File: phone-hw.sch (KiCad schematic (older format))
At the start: 45 parts

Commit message: connect RI to esp32
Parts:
- added R?: 10k, Resistor_SMD:R_0603_1608Metric_Pad1.05x0.95mm_HandSolder, symbol Device:R_Small_US
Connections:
- net labels added: GSM_RI, GSM_RI_2.8
- wire segments 333 -> 341
- no-connect marks 14 -> 11
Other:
- moved on the sheet: J?
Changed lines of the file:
@@
 F7 "DBG_RXD" I L 8450 1150 50
 F8 "PWRKEY" I R 9600 900 50
+F9 "RI" O R 9600 1300 50
 $EndSheet
 $Comp
@@
 	7450 4150 7450 4250
 Wire Wire Line
-	6900 4200 6900 4250
-Wire Wire Line
-	6900 4250 7100 4250
-Wire Wire Line
 	7100 4250 7450 4250
-Connection ~ 7100 4250
 $Comp
 L Device:R_Small_US R?
@@
 L power:VDD #PWR?
 U 1 1 5CF832E7
-P 4800 3500
-F 0 "#PWR?" H 4800 3350 50  0001 C CNN
-F 1 "VDD" H 4817 3673 50  0000 C CNN
-F 2 "" H 4800 3500 50  0001 C CNN
-F 3 "" H 4800 3500 50  0001 C CNN
-	1    4800 3500
+P 4800 3450
+F 0 "#PWR?" H 4800 3300 50  0001 C CNN
+F 1 "VDD" H 4817 3623 50  0000 C CNN
+F 2 "" H 4800 3450 50  0001 C CNN
+F 3 "" H 4800 3450 50  0001 C CNN
+	1    4800 3450
 	1    0    0    -1
 $EndComp
@@
 L power:+BATT #PWR?
 U 1 1 5CF9532A
-P 6900 4200
-F 0 "#PWR?" H 6900 4050 50  0001 C CNN
-F 1 "+BATT" H 6915 4373 50  0000 C CNN
-F 2 "" H 6900 4200 50  0001 C CNN
-F 3 "" H 6900 4200 50  0001 C CNN
-	1    6900 4200
+P 7750 4200
+F 0 "#PWR?" H 7750 4050 50  0001 C CNN
+F 1 "+BATT" H 7765 4373 50  0000 C CNN
+F 2 "" H 7750 4200 50  0001 C CNN
+F 3 "" H 7750 4200 50  0001 C CNN
+	1    7750 4200
 	1    0    0    -1
 $EndComp
 Wire Wire Line
 	6650 3600 7200 3600
-NoConn ~ 5850 4000
 NoConn ~ 5850 4100
 NoConn ~ 6650 4100
-NoConn ~ 6650 4000
 Wire Wire Line
 	8150 950  8250 950
@@
 Wire Wire Line
 	8400 4400 8400 4900
-Text GLabel 3550 4100 0    39   Output ~ 0
+Text GLabel 3900 4850 0    39   Output ~ 0
 JTAG_MTDO
-Text GLabel 3550 3900 0    39   Input ~ 0
+Text GLabel 3900 4650 0    39   Input ~ 0
 JTAG_MTCK
-Text GLabel 3550 4000 0    39   Input ~ 0
+Text GLabel 3900 4750 0    39   Input ~ 0
 JTAG_MTMS
-Text GLabel 3550 3800 0    39   Input ~ 0
+Text GLabel 3900 4550 0    39   Input ~ 0
 JTAG_MTDI
 Wire Wire Line
-	3550 4100 3600 4100
-Wire Wire Line
-	3600 4000 3550 4000
-Wire Wire Line
-	3550 3900 3600 3900
-Wire Wire Line
-	3550 3800 3600 3800
+	3900 4850 3950 4850
+Wire Wire Line
+	3950 4750 3900 4750
+Wire Wire Line
+	3900 4650 3950 4650
+Wire Wire Line
+	3900 4550 3950 4550
 $Comp
 L Connector_Generic:Conn_01x06 J?
 U 1 1 5D4CA230
-P 3800 3900
-F 0 "J?" H 4100 3950 50  0000 C CNN
-F 1 "Conn_01x06" H 4100 3850 50  0000 C CNN
-F 2 "Connector_PinHeader_2.54mm:PinHeader_1x06_P2.54mm_Vertical" H 3800 3900 50  0001 C CNN
-F 3 "~" H 3800 3900 50  0001 C CNN
-	1    3800 3900
+P 4150 4650
+F 0 "J?" H 4450 4700 50  0000 C CNN
+F 1 "Conn_01x06" H 4450 4600 50  0000 C CNN
+F 2 "Connector_PinHeader_2.54mm:PinHeader_1x06_P2.54mm_Vertical" H 4150 4650 50  0001 C CNN
+F 3 "~" H 4150 4650 50  0001 C CNN
+	1    4150 4650
 	1    0    0    -1
 $EndComp
@@
 L power:GND #PWR?
 U 1 1 5DC8B84C
-P 3550 4250
-F 0 "#PWR?" H 3550 4000 50  0001 C CNN
-F 1 "GND" H 3555 4077 50  0000 C CNN
-F 2 "" H 3550 4250 50  0001 C CNN
-F 3 "" H 3550 4250 50  0001 C CNN
-	1    3550 4250
-	1    0    0    -1
-$EndComp
-Wire Wire Line
-	3600 4200 3550 4200
-Wire Wire Line
-	3550 4200 3550 4250
+P 3900 5000
+F 0 "#PWR?" H 3900 4750 50  0001 C CNN
+F 1 "GND" H 3905 4827 50  0000 C CNN
+F 2 "" H 3900 5000 50  0001 C CNN
+F 3 "" H 3900 5000 50  0001 C CNN
+	1    3900 5000
+	1    0    0    -1
+$EndComp
+Wire Wire Line
+	3950 4950 3900 4950
+Wire Wire Line
+	3900 4950 3900 5000
 $Comp
 L power:VDD #PWR?
 U 1 1 5DCA34FE
-P 3550 3650
-F 0 "#PWR?" H 3550 3500 50  0001 C CNN
-F 1 "VDD" H 3567 3823 50  0000 C CNN
-F 2 "" H 3550 3650 50  0001 C CNN
-F 3 "" H 3550 3650 50  0001 C CNN
-	1    3550 3650
-	1    0    0    -1
-$EndComp
-Wire Wire Line
-	3600 3700 3550 3700
-Wire Wire Line
-	3550 3700 3550 3650
+P 3900 4400
+F 0 "#PWR?" H 3900 4250 50  0001 C CNN
+F 1 "VDD" H 3917 4573 50  0000 C CNN
+F 2 "" H 3900 4400 50  0001 C CNN
+F 3 "" H 3900 4400 50  0001 C CNN
+	1    3900 4400
+	1    0    0    -1
+$EndComp
+Wire Wire Line
+	3950 4450 3900 4450
+Wire Wire Line
+	3900 4450 3900 4400
 $Comp
 L Device:R_Small_US R?
@@
 	1    0    0    -1
 $EndComp
-NoConn ~ 2550 4800
+Text GLabel 9700 1300 2    39   Output ~ 0
+GSM_RI
+Wire Wire Line
+	9600 1300 9700 1300
+Text GLabel 6700 4000 2    39   Input ~ 0
+GSM_RI
+Wire Wire Line
+	7450 4250 7750 4250
+Wire Wire Line
+	7750 4250 7750 4200
+Connection ~ 7450 4250
+Wire Wire Line
+	6650 4000 6700 4000
+Text GLabel 4200 4000 0    39   Output ~ 0
+GSM_RI_2.8
+Wire Wire Line
+	5850 4000 4350 4000
+$Comp
+L Device:R_Small_US R?
+U 1 1 5DC1E4EB
+P 4350 3750
+F 0 "R?" H 4418 3796 50  0000 L CNN
+F 1 "10k" H 4418 3705 50  0000 L CNN
+F 2 "Resistor_SMD:R_0603_1608Metric_Pad1.05x0.95mm_HandSolder" H 4350 3750 50  0001 C CNN
+F 3 "~" H 4350 3750 50  0001 C CNN
+	1    4350 3750
+	-1   0    0    -1
+$EndComp
+Wire Wire Line
+	4350 4000 4350 3850
+Connection ~ 4350 4000
+Wire Wire Line
+	4350 4000 4200 4000
+Wire Wire Line
+	4800 3500 4350 3500
+Wire Wire Line
+	4350 3500 4350 3650
+Connection ~ 4800 3500
+Wire Wire Line
+	4800 3500 4800 3450
+Text GLabel 2550 4800 2    39   Input ~ 0
+GSM_RI_2.8
 $EndSCHEMATC

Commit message: annotate schematic and tweak some footprint associations
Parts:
- SW4, SW5, SW6: renamed from SW?; footprint Button_Switch_SMD:SW_SPST_EVQPE1 -> Button_Switch_THT:SW_Tactile_SPST_Angled_PTS645Vx58-2LFS
- U2: renamed from U?; footprint (none) -> Package_SO:TSSOP-24_4.4x7.8mm_P0.65mm
- gave numbers to parts that had none: 42

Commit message: change battery to use two different connectors instead of a small pin header
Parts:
- removed BT1: Battery_Cell, Connector_PinHeader_2.54mm:PinHeader_1x02_P2.54mm_Vertical, symbol Device:Battery_Cell
- added J5: BATT+, symbol Connector:Conn_01x01_Female
- added J6: BATT-, symbol Connector:Conn_01x01_Female
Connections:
- wire segments 341 -> 339
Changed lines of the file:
@@
 	2900 1050 2900 900
-Wire Wire Line
-	2300 900  2300 950
-$Comp
-L Device:Battery_Cell BT1
-U 1 1 5C9332A7
-P 2300 1150
-F 0 "BT1" H 2418 1246 50  0000 L CNN
-F 1 "Battery_Cell" H 2418 1155 50  0000 L CNN
-F 2 "Connector_PinHeader_2.54mm:PinHeader_1x02_P2.54mm_Vertical" V 2300 1210 50  0001 C CNN
-F 3 "~" V 2300 1210 50  0001 C CNN
-	1    2300 1150
-	1    0    0    -1
-$EndComp
-Wire Wire Line
-	2300 1250 2300 1300
 Wire Wire Line
 	2900 1300 2900 1150
@@
 Wire Wire Line
 	1200 4900 1250 4900
-Wire Wire Line
-	2300 900  2900 900
-Wire Wire Line
-	2300 1300 2900 1300
-$Comp
-L power:PWR_FLAG #FLG01
-U 1 1 5D6F8FE7
-P 1950 1250
-F 0 "#FLG01" H 1950 1325 50  0001 C CNN
-F 1 "PWR_FLAG" H 1950 1423 50  0000 C CNN
-F 2 "" H 1950 1250 50  0001 C CNN
-F 3 "~" H 1950 1250 50  0001 C CNN
-	1    1950 1250
-	1    0    0    -1
-$EndComp
-Wire Wire Line
-	2300 1300 1950 1300
-Wire Wire Line
-	1950 1300 1950 1250
-Connection ~ 2300 1300
 $Comp
 L power:PWR_FLAG #FLG03
@@
 Text GLabel 2550 4800 2    39   Input ~ 0
 GSM_RI_2.8
+$Comp
+L Connector:Conn_01x01_Female J5
+U 1 1 5DE9CCC6
+P 2100 900
+F 0 "J5" H 1992 675 50  0000 C CNN
+F 1 "BATT+" H 1992 766 50  0000 C CNN
+F 2 "" H 2100 900 50  0001 C CNN
+F 3 "~" H 2100 900 50  0001 C CNN
+	1    2100 900
+	-1   0    0    1
+$EndComp
+$Comp
+L Connector:Conn_01x01_Female J6
+U 1 1 5DF18DEB
+P 2100 1300
+F 0 "J6" H 1992 1075 50  0000 C CNN
+F 1 "BATT-" H 1992 1166 50  0000 C CNN
+F 2 "" H 2100 1300 50  0001 C CNN
+F 3 "~" H 2100 1300 50  0001 C CNN
+	1    2100 1300
+	-1   0    0    1
+$EndComp
+Wire Wire Line
+	2300 1300 2700 1300
+$Comp
+L power:PWR_FLAG #FLG0102
+U 1 1 5DF195A7
+P 2700 1200
+F 0 "#FLG0102" H 2700 1275 50  0001 C CNN
+F 1 "PWR_FLAG" H 2700 1373 50  0000 C CNN
+F 2 "" H 2700 1200 50  0001 C CNN
+F 3 "~" H 2700 1200 50  0001 C CNN
+	1    2700 1200
+	1    0    0    -1
+$EndComp
+Wire Wire Line
+	2700 1200 2700 1300
+Connection ~ 2700 1300
+Wire Wire Line
+	2700 1300 2900 1300
+Wire Wire Line
+	2300 900  2900 900
 $EndSCHEMATC

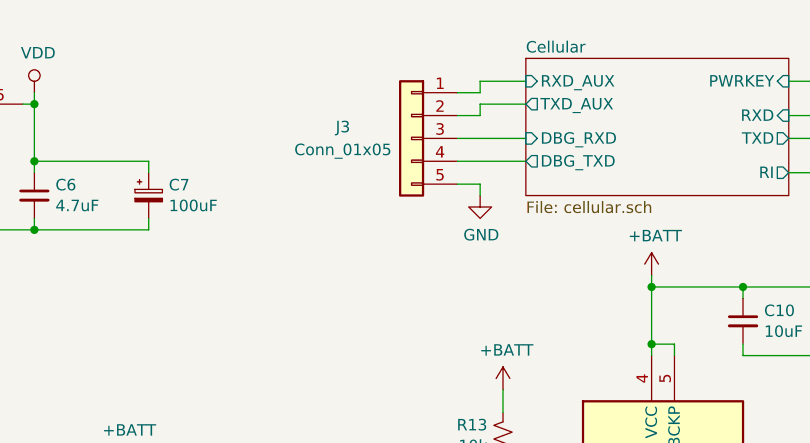
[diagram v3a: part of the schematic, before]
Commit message: remove debug port for modem
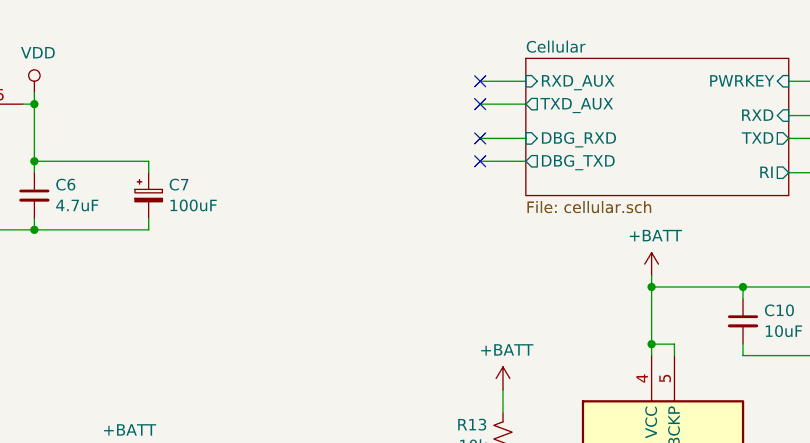
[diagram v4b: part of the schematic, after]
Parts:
- removed J3: Conn_01x05, Connector_PinHeader_2.54mm:PinHeader_1x05_P2.54mm_Vertical, symbol Connector_Generic:Conn_01x05
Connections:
- no-connect marks 11 -> 15
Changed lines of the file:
@@
 NoConn ~ 6650 4100
 Wire Wire Line
-	8150 950  8250 950
-Wire Wire Line
-	8250 950  8250 900
-Wire Wire Line
 	8250 900  8450 900
 Wire Wire Line
-	8150 1050 8250 1050
-Wire Wire Line
-	8250 1050 8250 1000
-Wire Wire Line
 	8250 1000 8450 1000
-Wire Wire Line
-	8150 1150 8450 1150
-Wire Wire Line
-	8150 1250 8450 1250
 $Comp
 L power:PWR_FLAG #FLG02
@@
 	-1   0    0    -1
 $EndComp
-$Comp
-L Connector_Generic:Conn_01x05 J3
-U 1 1 5D00D675
-P 7950 1150
-F 0 "J3" H 8250 1200 50  0000 C CNN
-F 1 "Conn_01x05" H 8250 1100 50  0000 C CNN
-F 2 "Connector_PinHeader_2.54mm:PinHeader_1x05_P2.54mm_Vertical" H 7950 1150 50  0001 C CNN
-F 3 "~" H 7950 1150 50  0001 C CNN
-	1    7950 1150
-	-1   0    0    -1
-$EndComp
-$Comp
-L power:GND #PWR044
-U 1 1 5DC175EF
-P 8250 1400
-F 0 "#PWR044" H 8250 1150 50  0001 C CNN
-F 1 "GND" H 8255 1227 50  0000 C CNN
-F 2 "" H 8250 1400 50  0001 C CNN
-F 3 "" H 8250 1400 50  0001 C CNN
-	1    8250 1400
-	1    0    0    -1
-$EndComp
-Wire Wire Line
-	8150 1350 8250 1350
-Wire Wire Line
-	8250 1350 8250 1400
 $Comp
 L power:GND #PWR016
@@
 Wire Wire Line
 	2300 900  2900 900
+Wire Wire Line
+	8450 1150 8250 1150
+Wire Wire Line
+	8450 1250 8250 1250
+NoConn ~ 8250 900
+NoConn ~ 8250 1000
+NoConn ~ 8250 1150
+NoConn ~ 8250 1250
 $EndSCHEMATC

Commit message: tweak some footprint associations
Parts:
- J2: footprint Connector_PinHeader_2.54mm:PinHeader_1x06_P2.54mm_Vertical -> Connector:Tag-Connect_TC2030-IDC-NL_2x03_P1.27mm_Vertical
- J5, J6: footprint (none) -> Connector_PinSocket_2.54mm:PinSocket_1x01_P2.54mm_Vertical
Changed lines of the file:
@@
 F 0 "J2" H 4450 4700 50  0000 C CNN
 F 1 "Conn_01x06" H 4450 4600 50  0000 C CNN
-F 2 "Connector_PinHeader_2.54mm:PinHeader_1x06_P2.54mm_Vertical" H 4150 4650 50  0001 C CNN
+F 2 "Connector:Tag-Connect_TC2030-IDC-NL_2x03_P1.27mm_Vertical" H 4150 4650 50  0001 C CNN
 F 3 "~" H 4150 4650 50  0001 C CNN
 	1    4150 4650
@@
 F 0 "J5" H 1992 675 50  0000 C CNN
 F 1 "BATT+" H 1992 766 50  0000 C CNN
-F 2 "" H 2100 900 50  0001 C CNN
+F 2 "Connector_PinSocket_2.54mm:PinSocket_1x01_P2.54mm_Vertical" H 2100 900 50  0001 C CNN
 F 3 "~" H 2100 900 50  0001 C CNN
 	1    2100 900
@@
 F 0 "J6" H 1992 1075 50  0000 C CNN
 F 1 "BATT-" H 1992 1166 50  0000 C CNN
-F 2 "" H 2100 1300 50  0001 C CNN
+F 2 "Connector_PinSocket_2.54mm:PinSocket_1x01_P2.54mm_Vertical" H 2100 1300 50  0001 C CNN
 F 3 "~" H 2100 1300 50  0001 C CNN
 	1    2100 1300

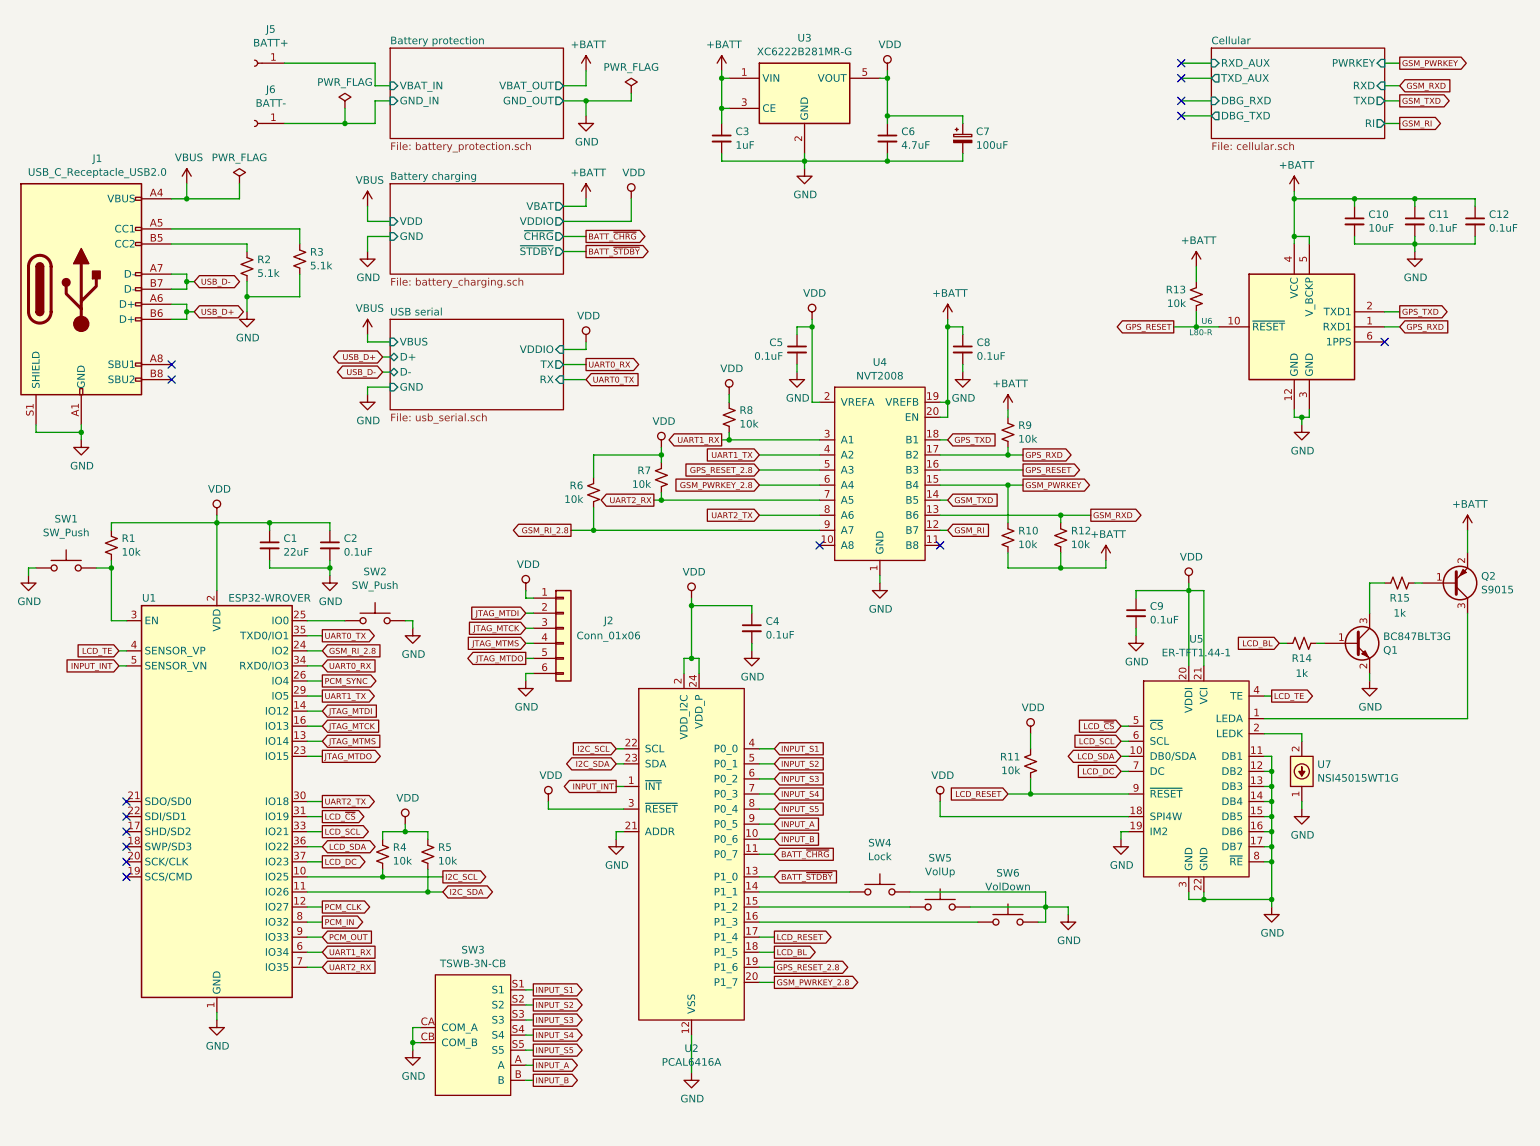
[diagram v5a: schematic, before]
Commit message: remove jtag port and move some other things around
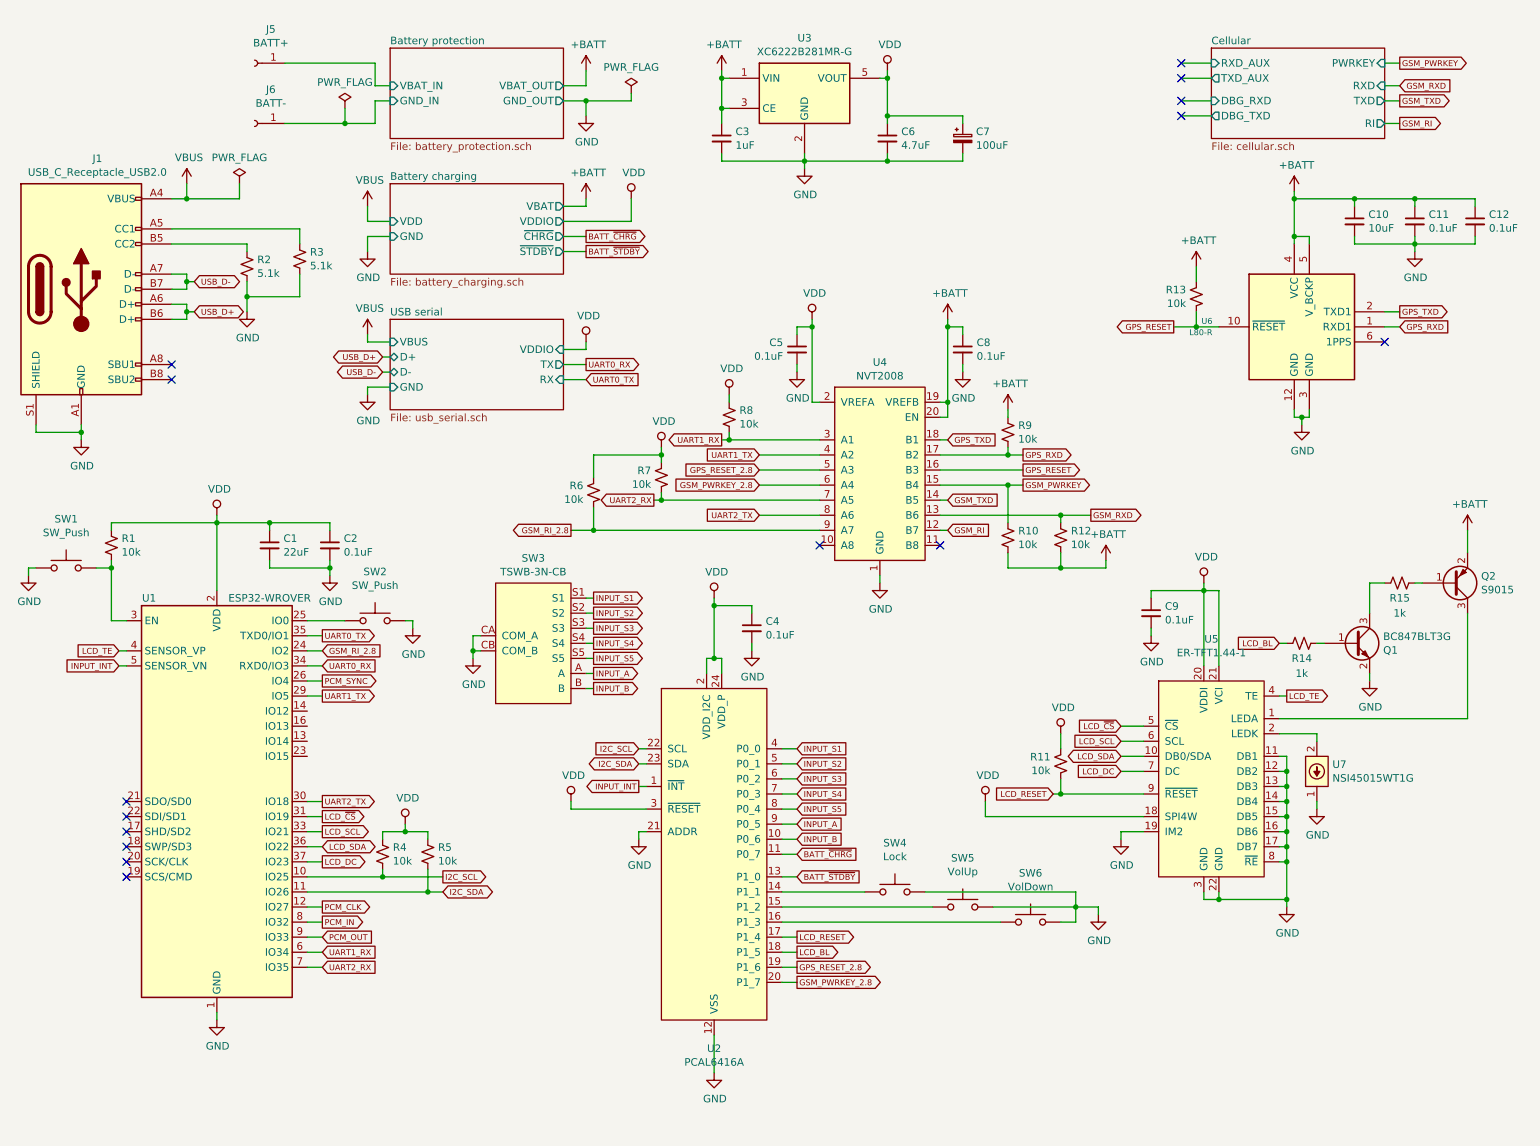
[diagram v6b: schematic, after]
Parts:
- removed J2: Conn_01x06, Connector:Tag-Connect_TC2030-IDC-NL_2x03_P1.27mm_Vertical, symbol Connector_Generic:Conn_01x06
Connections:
- net JTAG_MTCK: no longer names the net of U1.16 (IO13)
- net JTAG_MTDI: no longer names the net of U1.14 (IO12)
- net JTAG_MTDO: no longer names the net of U1.23 (IO15)
- net JTAG_MTMS: no longer names the net of U1.13 (IO14)
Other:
- moved on the sheet: C9, R11, SW3, SW4, SW5, SW6, U2, U5, U7
